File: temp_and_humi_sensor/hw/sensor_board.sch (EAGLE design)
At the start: 13 parts, among them U1 328P

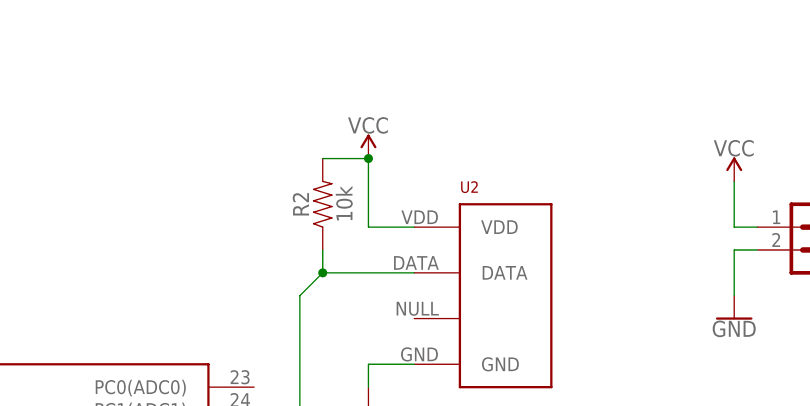
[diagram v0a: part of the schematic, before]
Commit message: Fixed power lines
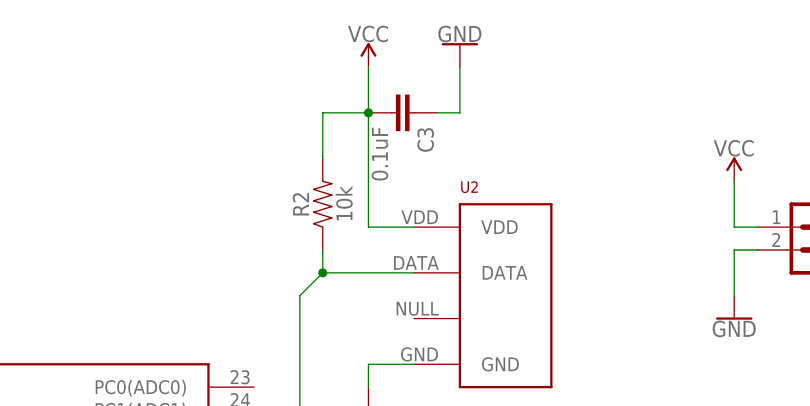
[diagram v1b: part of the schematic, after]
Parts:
- added C3: 0.1uF, SparkFun-Capacitors:0.1UF-KIT-EZ-50V-20%
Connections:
- net GND: now also C3.1
- net VCC: now also C3.2
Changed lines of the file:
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@@
 <part name="C1" library="SparkFun-Capacitors" deviceset="0.1UF" device="-KIT-EZ-50V-20%" value="0.1uF"/>
 <part name="J2" library="SparkFun-Connectors" deviceset="CONN_02" device=""/>
+<part name="C3" library="SparkFun-Capacitors" deviceset="0.1UF" device="-KIT-EZ-50V-20%" value="0.1uF"/>
+<part name="GND6" library="SparkFun-PowerSymbols" deviceset="GND" device=""/>
 </parts>
 <sheets>
@@
 <instance part="J4" gate="J$1" x="203.2" y="104.14" rot="R180"/>
 <instance part="U2" gate="G$1" x="167.64" y="127"/>
-<instance part="SUPPLY5" gate="G$1" x="152.4" y="142.24"/>
+<instance part="SUPPLY5" gate="G$1" x="152.4" y="152.4"/>
 <instance part="GND5" gate="1" x="152.4" y="114.3"/>
 <instance part="R2" gate="G$1" x="147.32" y="137.16" rot="R90"/>
 <instance part="C1" gate="G$1" x="78.74" y="91.44" rot="R180"/>
 <instance part="J2" gate="G$1" x="160.02" y="83.82" rot="R270"/>
+<instance part="C3" gate="G$1" x="154.94" y="147.32" rot="R270"/>
+<instance part="GND6" gate="1" x="162.56" y="154.94" rot="R180"/>
 </instances>
 <busses>
@@
 <pinref part="SUPPLY5" gate="G$1" pin="VCC"/>
 <wire x1="157.48" y1="134.62" x2="152.4" y2="134.62" width="0.1524" layer="91"/>
-<wire x1="152.4" y1="134.62" x2="152.4" y2="142.24" width="0.1524" layer="91"/>
+<wire x1="152.4" y1="134.62" x2="152.4" y2="147.32" width="0.1524" layer="91"/>
 <pinref part="R2" gate="G$1" pin="2"/>
-<wire x1="147.32" y1="142.24" x2="152.4" y2="142.24" width="0.1524" layer="91"/>
-<junction x="152.4" y="142.24"/>
+<wire x1="152.4" y1="147.32" x2="152.4" y2="152.4" width="0.1524" layer="91"/>
+<wire x1="147.32" y1="142.24" x2="147.32" y2="147.32" width="0.1524" layer="91"/>
+<wire x1="147.32" y1="147.32" x2="152.4" y2="147.32" width="0.1524" layer="91"/>
+<junction x="152.4" y="147.32"/>
+<pinref part="C3" gate="G$1" pin="2"/>
 </segment>
 </net>
@@
 <junction x="91.44" y="63.5"/>
 </segment>
+<segment>
+<pinref part="C3" gate="G$1" pin="1"/>
+<pinref part="GND6" gate="1" pin="GND"/>
+<wire x1="160.02" y1="147.32" x2="162.56" y2="147.32" width="0.1524" layer="91"/>
+<wire x1="162.56" y1="147.32" x2="162.56" y2="152.4" width="0.1524" layer="91"/>
+</segment>
 </net>

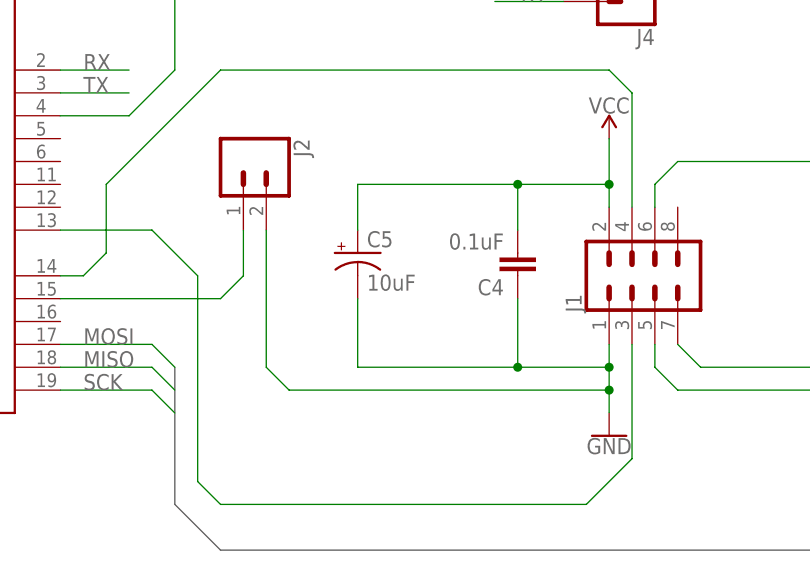
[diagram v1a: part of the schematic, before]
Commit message: Added bigger capacitor
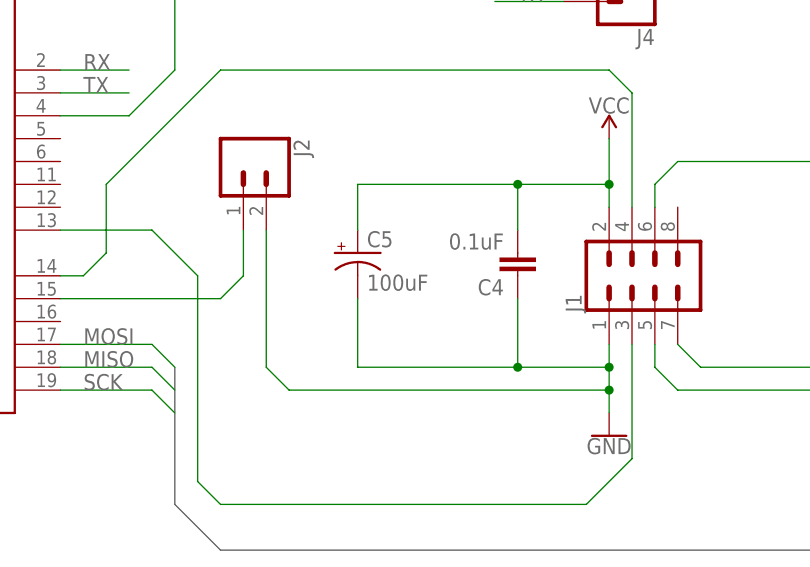
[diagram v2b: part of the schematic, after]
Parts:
- C5: value 10uF -> 100uF; device SparkFun-Capacitors:10UF-POLAR-RADIAL-2.5MM-25V-20% -> SparkFun-Capacitors:100UF-POLAR-RADIAL-2.5MM-25V-20%
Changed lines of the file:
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@@
 <part name="GND3" library="SparkFun-PowerSymbols" deviceset="GND" device=""/>
 <part name="C4" library="SparkFun-Capacitors" deviceset="0.1UF" device="-KIT-EZ-50V-20%" value="0.1uF"/>
-<part name="C5" library="SparkFun-Capacitors" deviceset="10UF-POLAR" device="-RADIAL-2.5MM-25V-20%" value="10uF"/>
 <part name="GND4" library="SparkFun-PowerSymbols" deviceset="GND" device=""/>
 <part name="SUPPLY3" library="SparkFun-PowerSymbols" deviceset="VCC" device=""/>
@@
 <part name="C3" library="SparkFun-Capacitors" deviceset="0.1UF" device="-KIT-EZ-50V-20%" value="0.1uF"/>
 <part name="GND6" library="SparkFun-PowerSymbols" deviceset="GND" device=""/>
+<part name="C5" library="SparkFun-Capacitors" deviceset="100UF-POLAR" device="-RADIAL-2.5MM-25V-20%" value="100uF"/>
 </parts>
 <sheets>
@@
 <instance part="GND3" gate="1" x="200.66" y="53.34"/>
 <instance part="C4" gate="G$1" x="190.5" y="73.66" rot="R180"/>
-<instance part="C5" gate="G$1" x="172.72" y="73.66"/>
 <instance part="GND4" gate="1" x="55.88" y="93.98"/>
 <instance part="SUPPLY3" gate="G$1" x="55.88" y="137.16"/>
@@
 <instance part="C3" gate="G$1" x="154.94" y="147.32" rot="R270"/>
 <instance part="GND6" gate="1" x="162.56" y="154.94" rot="R180"/>
+<instance part="C5" gate="G$1" x="172.72" y="73.66"/>
 </instances>
 <busses>
@@
 <wire x1="200.66" y1="81.28" x2="190.5" y2="81.28" width="0.1524" layer="91"/>
 <junction x="200.66" y="81.28"/>
-<pinref part="C5" gate="G$1" pin="+"/>
 <wire x1="190.5" y1="81.28" x2="172.72" y2="81.28" width="0.1524" layer="91"/>
 <wire x1="172.72" y1="81.28" x2="172.72" y2="76.2" width="0.1524" layer="91"/>
@@
 <wire x1="190.5" y1="76.2" x2="190.5" y2="81.28" width="0.1524" layer="91"/>
 <junction x="190.5" y="81.28"/>
+<pinref part="C5" gate="G$1" pin="+"/>
 </segment>
 <segment>
@@
 <wire x1="200.66" y1="60.96" x2="190.5" y2="60.96" width="0.1524" layer="91"/>
 <junction x="200.66" y="60.96"/>
-<pinref part="C5" gate="G$1" pin="-"/>
 <wire x1="190.5" y1="60.96" x2="172.72" y2="60.96" width="0.1524" layer="91"/>
 <wire x1="172.72" y1="68.58" x2="172.72" y2="60.96" width="0.1524" layer="91"/>
@@
 <wire x1="165.1" y1="58.42" x2="200.66" y2="58.42" width="0.1524" layer="91"/>
 <junction x="200.66" y="58.42"/>
+<pinref part="C5" gate="G$1" pin="-"/>
 </segment>
 <segment>
